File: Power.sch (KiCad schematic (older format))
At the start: 1 part

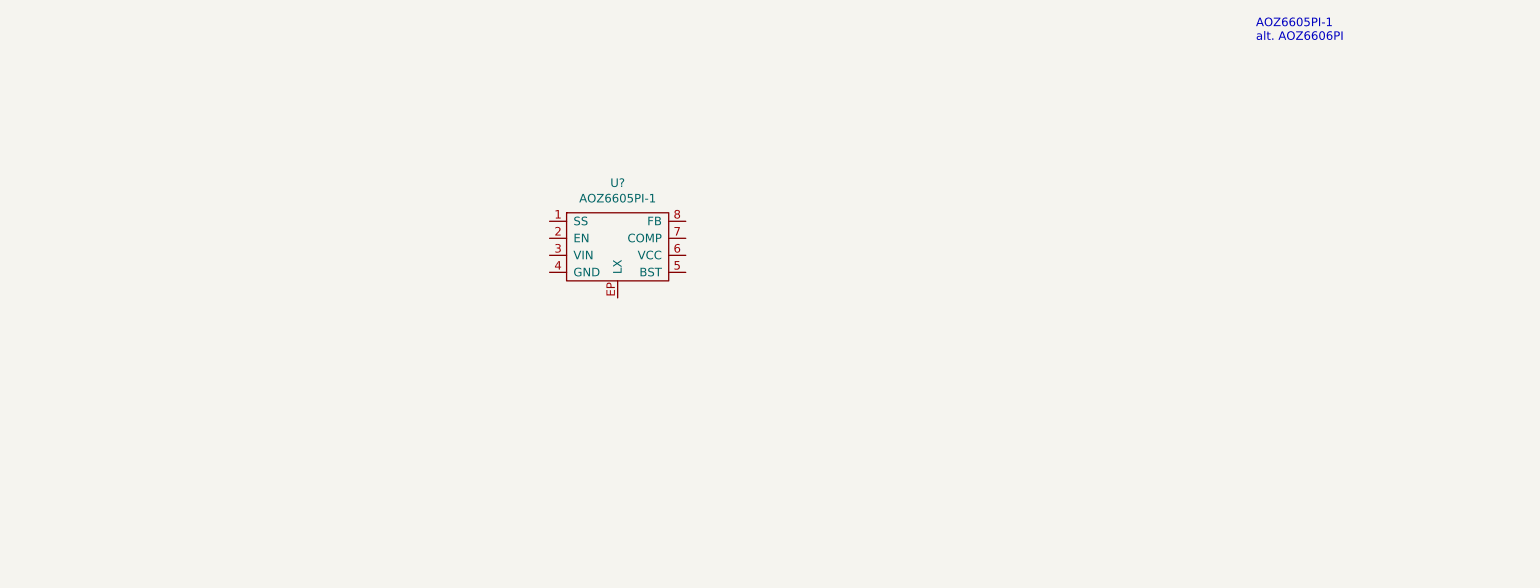
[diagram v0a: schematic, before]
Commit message: Setting up fields, more structure, touching up schematic display properties.
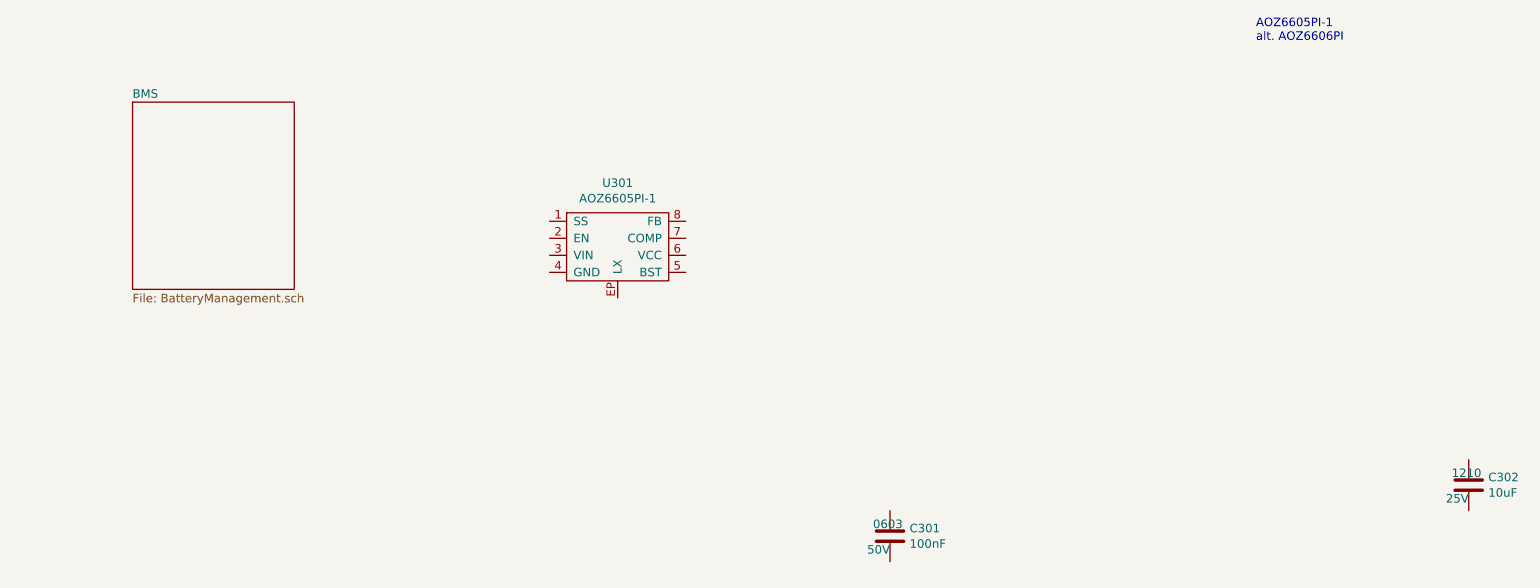
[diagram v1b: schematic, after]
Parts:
- added C301: 100nF, Capacitor_SMD:C_0603_1608Metric_Pad1.05x0.95mm_HandSolder, symbol Device:C
- added C302: 10uF, Capacitors_SMD:C_1210_HandSoldering, symbol Device:C
- U301: renamed from U?; Link (none) -> https://www.digikey.com.au/product-detail/en/alpha-omega-se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; Manufacturer (none) -> A&O; Mfg Part # (none) -> AOZ6605PI-1; Supplier 1 (none) -> Digi-Key; Supplier Part Number 1 (none) -> 785-1853-1-ND; Unit Cost A$ (none) -> 0.96000
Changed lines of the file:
@@
 $Descr A4 11693 8268
 encoding utf-8
-Sheet 2 2
+Sheet 2 3
 Title ""
 Date ""
@@
 P 4750 3000
 AR Path="/5DA994B6" Ref="U?"  Part="1"
-AR Path="/5DA95EB0/5DA994B6" Ref="U?"  Part="1"
-F 0 "U?" H 4750 3375 50  0000 C CNN
+AR Path="/5DA95EB0/5DA994B6" Ref="U301"  Part="1"
+F 0 "U301" H 4750 3375 50  0000 C CNN
 F 1 "AOZ6605PI-1" H 4750 3284 50  0000 C CNN
 F 2 "" H 4850 3000 50  0001 C CNN
-F 3 "" H 4850 3000 50  0001 C CNN
+F 3 "http://www.aosmd.com/res/data_sheets/AOZ6605PI-1.pdf" H 4850 3000 50  0001 C CNN
+F 4 "https://www.digikey.com.au/product-detail/en/alpha-omega-semiconductor-inc/AOZ6605PI-1/785-1853-1-ND/10258148" H 4750 3000 50  0001 C CNN "Link"
+F 5 "A&O" H 4750 3000 50  0001 C CNN "Manufacturer"
+F 6 "AOZ6605PI-1" H 4750 3000 50  0001 C CNN "Mfg Part #"
+F 7 "Digi-Key" H 4750 3000 50  0001 C CNN "Supplier 1"
+F 8 "785-1853-1-ND" H 4750 3000 50  0001 C CNN "Supplier Part Number 1"
+F 9 "0.96000" H 4750 3000 50  0001 C CNN "Unit Cost A$"
 	1    4750 3000
 	1    0    0    -1
 $EndComp
+$Sheet
+S 1900 2150 950  1100
+U 5DAAD200
+F0 "BMS" 50
+F1 "BatteryManagement.sch" 50
+$EndSheet
+$Comp
+L Device:C C?
+U 1 1 5DB90873
+P 9750 4400
+AR Path="/5DB90873" Ref="C?"  Part="1"
+AR Path="/5DA95EB0/5DB90873" Ref="C302"  Part="1"
+F 0 "C302" H 9865 4446 50  0000 L CNN
+F 1 "10uF" H 9865 4355 50  0000 L CNN
+F 2 "Capacitors_SMD:C_1210_HandSoldering" H 9788 4250 50  0001 C CNN
+F 3 "~" H 9750 4400 50  0001 C CNN
+F 4 "1210" H 9650 4500 50  0000 L TNN "Package"
+F 5 "Digi-Key" H 9750 4400 50  0001 C CNN "Supplier 1"
+F 6 "1276-1854-1-ND" H 9750 4400 50  0001 C CNN "Supplier Part Number 1"
+F 7 "CAP CER 10UF 25V X5R 1210" H 9750 4400 50  0001 C CNN "Description"
+F 8 "25V" H 9750 4350 50  0000 R TNN "Voltage Rating"
+F 9 "https://www.digikey.com/product-detail/en/samsung-electro-mechanics/CL32A106KAULNNE/1276-1854-1-ND/3889940" H 9750 4400 50  0001 C CNN "Link"
+F 10 "0.46000" H 9750 4400 50  0001 C CNN "Unit Cost A$"
+	1    9750 4400
+	1    0    0    -1
+$EndComp
+$Comp
+L Device:C C?
+U 1 1 5DB8C583
+P 6350 4700
+AR Path="/5DB8C583" Ref="C?"  Part="1"
+AR Path="/5DA95EB0/5DB8C583" Ref="C301"  Part="1"
+F 0 "C301" H 6465 4746 50  0000 L CNN
+F 1 "100nF" H 6465 4655 50  0000 L CNN
+F 2 "Capacitor_SMD:C_0603_1608Metric_Pad1.05x0.95mm_HandSolder" H 6388 4550 50  0001 C CNN
+F 3 "~" H 6350 4700 50  0001 C CNN
+F 4 "0603" H 6250 4800 50  0000 L TNN "Package"
+F 5 "CAP CER 0.1UF 50V X7R 0603" H 6350 4700 50  0001 C CNN "Description"
+F 6 "50V" H 6350 4650 50  0000 R TNN "Voltage Rating"
+F 7 "https://www.digikey.com/product-detail/en/samsung-electro-mechanics/CL10B104KB8NNNC/1276-1000-1-ND/3889086" H 6350 4700 50  0001 C CNN "Link"
+F 8 "Digi-Key" H 6350 4700 50  0001 C CNN "Supplier 1"
+F 9 "1276-1000-1-ND" H 6350 4700 50  0001 C CNN "Supplier Part Number 1"
+F 10 "0.15000" H 6350 4700 50  0001 C CNN "Unit Cost A$"
+	1    6350 4700
+	1    0    0    -1
+$EndComp

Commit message: Decisions on DCDC, adding components.
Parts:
- added L301: L_Small, symbol Device:L_Small
- added R?: R_Small_US, symbol Device:R_Small_US
- C302: footprint Capacitors_SMD:C_1210_HandSoldering -> Capacitors_SMD:C_1210
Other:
- note added: "alt. AOZ6606PI"
- note removed: "AOZ6605PI-1\nalt. AOZ6606PI"
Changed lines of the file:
@@
 Comment4 ""
 $EndDescr
-Text Notes 8500 1800 0    50   ~ 0
-AOZ6605PI-1\nalt. AOZ6606PI
+Text Notes 5000 2650 0    50   ~ 0
+alt. AOZ6606PI
 $Comp
 L dingo-hat:AOZ6605PI-1 U?
@@
 F 0 "C302" H 9865 4446 50  0000 L CNN
 F 1 "10uF" H 9865 4355 50  0000 L CNN
-F 2 "Capacitors_SMD:C_1210_HandSoldering" H 9788 4250 50  0001 C CNN
+F 2 "Capacitors_SMD:C_1210" H 9788 4250 50  0001 C CNN
 F 3 "~" H 9750 4400 50  0001 C CNN
 F 4 "1210" H 9650 4500 50  0000 L TNN "Package"
@@
 	1    0    0    -1
 $EndComp
+$Comp
+L Device:L_Small L301
+U 1 1 5DBD6690
+P 7300 3300
+F 0 "L301" V 7485 3300 50  0000 C CNN
+F 1 "L_Small" V 7394 3300 50  0000 C CNN
+F 2 "" H 7300 3300 50  0001 C CNN
+F 3 "~" H 7300 3300 50  0001 C CNN
+F 4 "FIXED IND 3.3UH 7.8A 19 MOHM SMD" H 7300 3300 50  0001 C CNN "Description"
+F 5 "https://www.digikey.com.au/product-detail/en/kemet/MPLCH0740L3R3/399-10991-1-ND/4506443" H 7300 3300 50  0001 C CNN "Link"
+F 6 "KEMET" H 7300 3300 50  0001 C CNN "Manufacturer"
+F 7 "399-10991-1-ND" H 7300 3300 50  0001 C CNN "Supplier Part Number 1"
+F 8 "1.42000" H 7300 3300 50  0001 C CNN "Unit Cost A$"
+	1    7300 3300
+	0    -1   -1   0
+$EndComp
+$Comp
+L Device:R_Small_US R?
+U 1 1 5DBD8784
+P 3950 3850
+F 0 "R?" H 4018 3896 50  0000 L CNN
+F 1 "R_Small_US" H 4018 3805 50  0000 L CNN
+F 2 "" H 3950 3850 50  0001 C CNN
+F 3 "~" H 3950 3850 50  0001 C CNN
+	1    3950 3850
+	1    0    0    -1
+$EndComp

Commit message: Doing schematic of DCDC.
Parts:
- added C303: 10uF, Capacitors_SMD:C_1206, symbol Device:C
- added C304: 22nF, Capacitors_SMD:C_0603, symbol Device:C
- added C305: 47uF, libs:CP_Elec_6.6x6.6, symbol Device:CP1_Small
- added C?: 100nF, Capacitors_SMD:C_0603, symbol Device:C
- added C?: DNF, Capacitors_SMD:C_0603, symbol Device:C
- added R302: 15k, Resistors_SMD:R_0603, symbol Device:R_Small_US
- added R?: 0R, Resistors_SMD:R_0603, symbol Device:R_Small_US
- added R?: DNF, Resistors_SMD:R_0603, symbol Device:R_Small_US
- C301: footprint Capacitor_SMD:C_0603_1608Metric_Pad1.05x0.95mm_HandSolder -> Capacitors_SMD:C_0603
- L301: value L_Small -> 3.3uH; DCR (none) -> 19mOhm
- R301: renamed from R?; value R_Small_US -> 110k; footprint (none) -> Resistors_SMD:R_0603
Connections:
- net labels added: GND
- wire segments 0 -> 32
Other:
- moved on the sheet: C301, C302, L301, R301

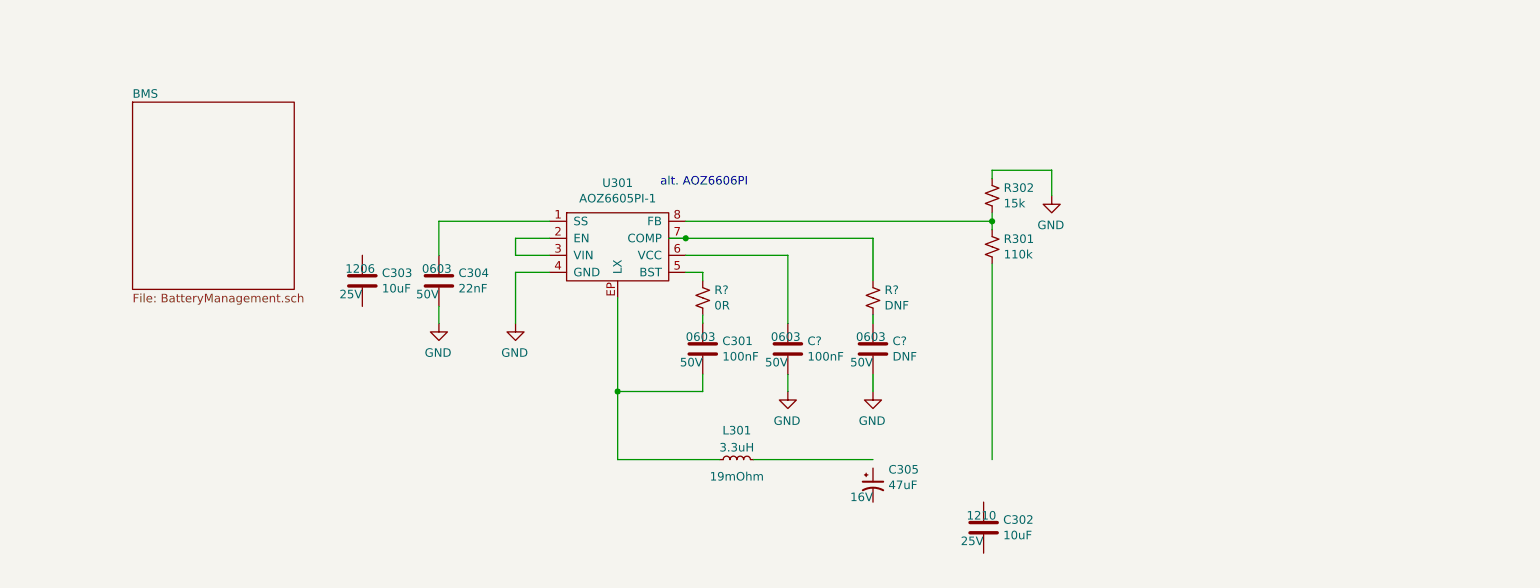
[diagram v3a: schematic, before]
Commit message: Starting battery protection & management.
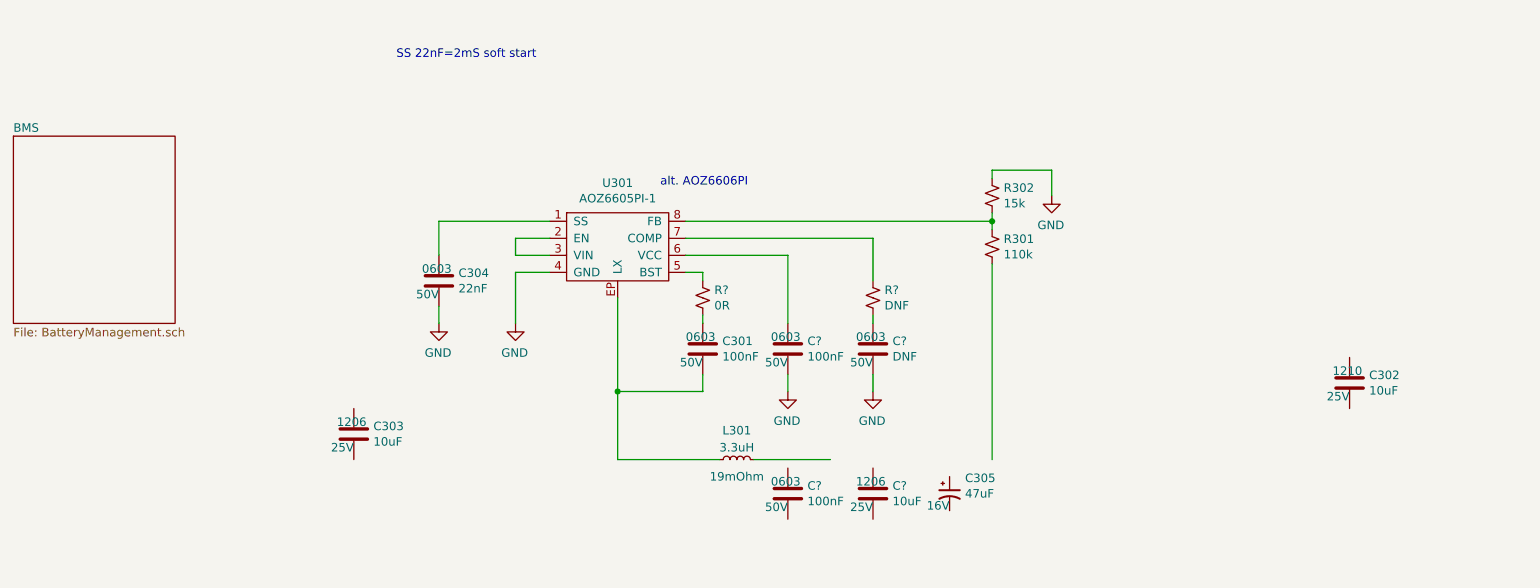
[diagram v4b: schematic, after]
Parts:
- added C?: 100nF, Capacitors_SMD:C_0603, symbol Device:C
- added C?: 10uF, Capacitors_SMD:C_1206, symbol Device:C
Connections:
- wire segments 32 -> 31
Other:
- note added: "SS 22nF=2mS soft start"
- moved on the sheet: C302, C303, C305
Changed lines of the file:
@@
 $EndComp
 $Sheet
-S 1900 2150 950  1100
+S 1200 2350 950  1100
 U 5DAAD200
 F0 "BMS" 50
@@
 L Device:C C?
 U 1 1 5DBE1F8A
-P 3250 3200
+P 3200 4100
 AR Path="/5DBE1F8A" Ref="C?"  Part="1"
 AR Path="/5DA95EB0/5DBE1F8A" Ref="C303"  Part="1"
-F 0 "C303" H 3365 3246 50  0000 L CNN
-F 1 "10uF" H 3365 3155 50  0000 L CNN
-F 2 "Capacitors_SMD:C_1206" H 3288 3050 50  0001 C CNN
-F 3 "~" H 3250 3200 50  0001 C CNN
-F 4 "1206" H 3150 3300 50  0000 L TNN "Package"
-F 5 "CAP CER 10UF 25V X5R 1206" H 3250 3200 50  0001 C CNN "Description"
-F 6 "25V" H 3250 3150 50  0000 R TNN "Voltage Rating"
-F 7 "https://www.digikey.com.au/product-detail/en/samsung-electro-mechanics/CL31A106KAHNNNE/1276-1075-1-ND/3889161" H 3250 3200 50  0001 C CNN "Link"
-F 8 "Digi-Key" H 3250 3200 50  0001 C CNN "Supplier 1"
-F 9 "1276-1075-1-ND" H 3250 3200 50  0001 C CNN "Supplier Part Number 1"
-F 10 "0.34000" H 3250 3200 50  0001 C CNN "Unit Cost A$"
-	1    3250 3200
+F 0 "C303" H 3315 4146 50  0000 L CNN
+F 1 "10uF" H 3315 4055 50  0000 L CNN
+F 2 "Capacitors_SMD:C_1206" H 3238 3950 50  0001 C CNN
+F 3 "~" H 3200 4100 50  0001 C CNN
+F 4 "1206" H 3100 4200 50  0000 L TNN "Package"
+F 5 "CAP CER 10UF 25V X5R 1206" H 3200 4100 50  0001 C CNN "Description"
+F 6 "25V" H 3200 4050 50  0000 R TNN "Voltage Rating"
+F 7 "https://www.digikey.com.au/product-detail/en/samsung-electro-mechanics/CL31A106KAHNNNE/1276-1075-1-ND/3889161" H 3200 4100 50  0001 C CNN "Link"
+F 8 "Digi-Key" H 3200 4100 50  0001 C CNN "Supplier 1"
+F 9 "1276-1075-1-ND" H 3200 4100 50  0001 C CNN "Supplier Part Number 1"
+F 10 "0.34000" H 3200 4100 50  0001 C CNN "Unit Cost A$"
+	1    3200 4100
 	1    0    0    -1
 $EndComp
@@
 L Device:CP1_Small C305
 U 1 1 5DBE36A3
-P 6250 4400
-F 0 "C305" H 6341 4491 50  0000 L CNN
-F 1 "47uF" H 6341 4400 50  0000 L CNN
-F 2 "libs:CP_Elec_6.6x6.6" H 6250 4400 50  0001 C CNN
-F 3 "~" H 6250 4400 50  0001 C CNN
-F 4 "CAP ALUM 47UF 20% 25V SMD" H 6250 4400 50  0001 C CNN "Description"
-F 5 "https://www.digikey.com.au/product-detail/en/panasonic-electronic-components/EEE-HC1E470XP/PCE3753CT-ND/672807" H 6250 4400 50  0001 C CNN "Link"
-F 6 "Panasonic Electronic Components" H 6250 4400 50  0001 C CNN "Manufacturer"
-F 7 "Radial, Can - SMD 6.6x6.6" H 6250 4400 50  0001 C CNN "Package"
-F 8 "PCE3753CT-ND" H 6250 4400 50  0001 C CNN "Supplier Part Number 1"
-F 9 "0.20000" H 6250 4400 50  0001 C CNN "Unit Cost A$"
-F 10 "Digi-Key" H 6250 4400 50  0001 C CNN "Supplier 1"
-F 11 "16V" H 6250 4300 50  0000 R BNN "Voltage Rating"
-	1    6250 4400
+P 6700 4450
+F 0 "C305" H 6791 4541 50  0000 L CNN
+F 1 "47uF" H 6791 4450 50  0000 L CNN
+F 2 "libs:CP_Elec_6.6x6.6" H 6700 4450 50  0001 C CNN
+F 3 "~" H 6700 4450 50  0001 C CNN
+F 4 "CAP ALUM 47UF 20% 25V SMD" H 6700 4450 50  0001 C CNN "Description"
+F 5 "https://www.digikey.com.au/product-detail/en/panasonic-electronic-components/EEE-HC1E470XP/PCE3753CT-ND/672807" H 6700 4450 50  0001 C CNN "Link"
+F 6 "Panasonic Electronic Components" H 6700 4450 50  0001 C CNN "Manufacturer"
+F 7 "Radial, Can - SMD 6.6x6.6" H 6700 4450 50  0001 C CNN "Package"
+F 8 "PCE3753CT-ND" H 6700 4450 50  0001 C CNN "Supplier Part Number 1"
+F 9 "0.20000" H 6700 4450 50  0001 C CNN "Unit Cost A$"
+F 10 "Digi-Key" H 6700 4450 50  0001 C CNN "Supplier 1"
+F 11 "16V" H 6700 4350 50  0000 R BNN "Voltage Rating"
+	1    6700 4450
 	1    0    0    -1
 $EndComp
@@
 	4750 4250 5350 4250
 Wire Wire Line
-	5550 4250 6250 4250
+	5550 4250 6000 4250
 Wire Wire Line
 	6950 4250 6950 3100
@@
 L Device:C C?
 U 1 1 5DB90873
-P 6900 4650
+P 9050 3800
 AR Path="/5DB90873" Ref="C?"  Part="1"
 AR Path="/5DA95EB0/5DB90873" Ref="C302"  Part="1"
-F 0 "C302" H 7015 4696 50  0000 L CNN
-F 1 "10uF" H 7015 4605 50  0000 L CNN
-F 2 "Capacitors_SMD:C_1210" H 6938 4500 50  0001 C CNN
-F 3 "~" H 6900 4650 50  0001 C CNN
-F 4 "1210" H 6800 4750 50  0000 L TNN "Package"
-F 5 "Digi-Key" H 6900 4650 50  0001 C CNN "Supplier 1"
-F 6 "1276-1854-1-ND" H 6900 4650 50  0001 C CNN "Supplier Part Number 1"
-F 7 "CAP CER 10UF 25V X5R 1210" H 6900 4650 50  0001 C CNN "Description"
-F 8 "25V" H 6900 4600 50  0000 R TNN "Voltage Rating"
-F 9 "https://www.digikey.com/product-detail/en/samsung-electro-mechanics/CL32A106KAULNNE/1276-1854-1-ND/3889940" H 6900 4650 50  0001 C CNN "Link"
-F 10 "0.46000" H 6900 4650 50  0001 C CNN "Unit Cost A$"
-	1    6900 4650
+F 0 "C302" H 9165 3846 50  0000 L CNN
+F 1 "10uF" H 9165 3755 50  0000 L CNN
+F 2 "Capacitors_SMD:C_1210" H 9088 3650 50  0001 C CNN
+F 3 "~" H 9050 3800 50  0001 C CNN
+F 4 "1210" H 8950 3900 50  0000 L TNN "Package"
+F 5 "Digi-Key" H 9050 3800 50  0001 C CNN "Supplier 1"
+F 6 "1276-1854-1-ND" H 9050 3800 50  0001 C CNN "Supplier Part Number 1"
+F 7 "CAP CER 10UF 25V X5R 1210" H 9050 3800 50  0001 C CNN "Description"
+F 8 "25V" H 9050 3750 50  0000 R TNN "Voltage Rating"
+F 9 "https://www.digikey.com/product-detail/en/samsung-electro-mechanics/CL32A106KAULNNE/1276-1854-1-ND/3889940" H 9050 3800 50  0001 C CNN "Link"
+F 10 "0.46000" H 9050 3800 50  0001 C CNN "Unit Cost A$"
+	1    9050 3800
 	1    0    0    -1
 $EndComp
@@
 	6250 2950 6250 3200
 Wire Wire Line
-	5050 2950 5150 2950
-Wire Wire Line
 	6250 3400 6250 3450
 Wire Wire Line
 	6250 3750 6250 3850
-Connection ~ 5150 2950
 Wire Wire Line
 	5150 2950 6250 2950
@@
 Wire Wire Line
 	3700 2850 4350 2850
+Text Notes 3450 1900 0    50   ~ 0
+SS 22nF=2mS soft start
+$Comp
+L Device:C C?
+U 1 1 5DC061BD
+P 5750 4450
+AR Path="/5DC061BD" Ref="C?"  Part="1"
+AR Path="/5DA95EB0/5DC061BD" Ref="C?"  Part="1"
+F 0 "C?" H 5865 4496 50  0000 L CNN
+F 1 "100nF" H 5865 4405 50  0000 L CNN
+F 2 "Capacitors_SMD:C_0603" H 5788 4300 50  0001 C CNN
+F 3 "~" H 5750 4450 50  0001 C CNN
+F 4 "0603" H 5650 4550 50  0000 L TNN "Package"
+F 5 "CAP CER 0.1UF 50V X7R 0603" H 5750 4450 50  0001 C CNN "Description"
+F 6 "50V" H 5750 4400 50  0000 R TNN "Voltage Rating"
+F 7 "https://www.digikey.com/product-detail/en/samsung-electro-mechanics/CL10B104KB8NNNC/1276-1000-1-ND/3889086" H 5750 4450 50  0001 C CNN "Link"
+F 8 "Digi-Key" H 5750 4450 50  0001 C CNN "Supplier 1"
+F 9 "1276-1000-1-ND" H 5750 4450 50  0001 C CNN "Supplier Part Number 1"
+F 10 "0.15000" H 5750 4450 50  0001 C CNN "Unit Cost A$"
+	1    5750 4450
+	1    0    0    -1
+$EndComp
+$Comp
+L Device:C C?
+U 1 1 5DC081D7
+P 6250 4450
+AR Path="/5DC081D7" Ref="C?"  Part="1"
+AR Path="/5DA95EB0/5DC081D7" Ref="C?"  Part="1"
+F 0 "C?" H 6365 4496 50  0000 L CNN
+F 1 "10uF" H 6365 4405 50  0000 L CNN
+F 2 "Capacitors_SMD:C_1206" H 6288 4300 50  0001 C CNN
+F 3 "~" H 6250 4450 50  0001 C CNN
+F 4 "1206" H 6150 4550 50  0000 L TNN "Package"
+F 5 "CAP CER 10UF 25V X5R 1206" H 6250 4450 50  0001 C CNN "Description"
+F 6 "25V" H 6250 4400 50  0000 R TNN "Voltage Rating"
+F 7 "https://www.digikey.com.au/product-detail/en/samsung-electro-mechanics/CL31A106KAHNNNE/1276-1075-1-ND/3889161" H 6250 4450 50  0001 C CNN "Link"
+F 8 "Digi-Key" H 6250 4450 50  0001 C CNN "Supplier 1"
+F 9 "1276-1075-1-ND" H 6250 4450 50  0001 C CNN "Supplier Part Number 1"
+F 10 "0.34000" H 6250 4450 50  0001 C CNN "Unit Cost A$"
+	1    6250 4450
+	1    0    0    -1
+$EndComp
 $EndSCHEMATC
